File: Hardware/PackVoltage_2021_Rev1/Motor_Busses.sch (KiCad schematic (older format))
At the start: 40 parts, among them Q1 Q_NMOS_DGS, Q2 Q_NMOS_DGS, Q3 Q_NMOS_DGS, Q4 Q_NMOS_DGS, U2 LT1910, U3 LT1910, U4 LT1910, U5 INA281, U6 INA281, U7 INA281, U8 LT1910, U9 INA281

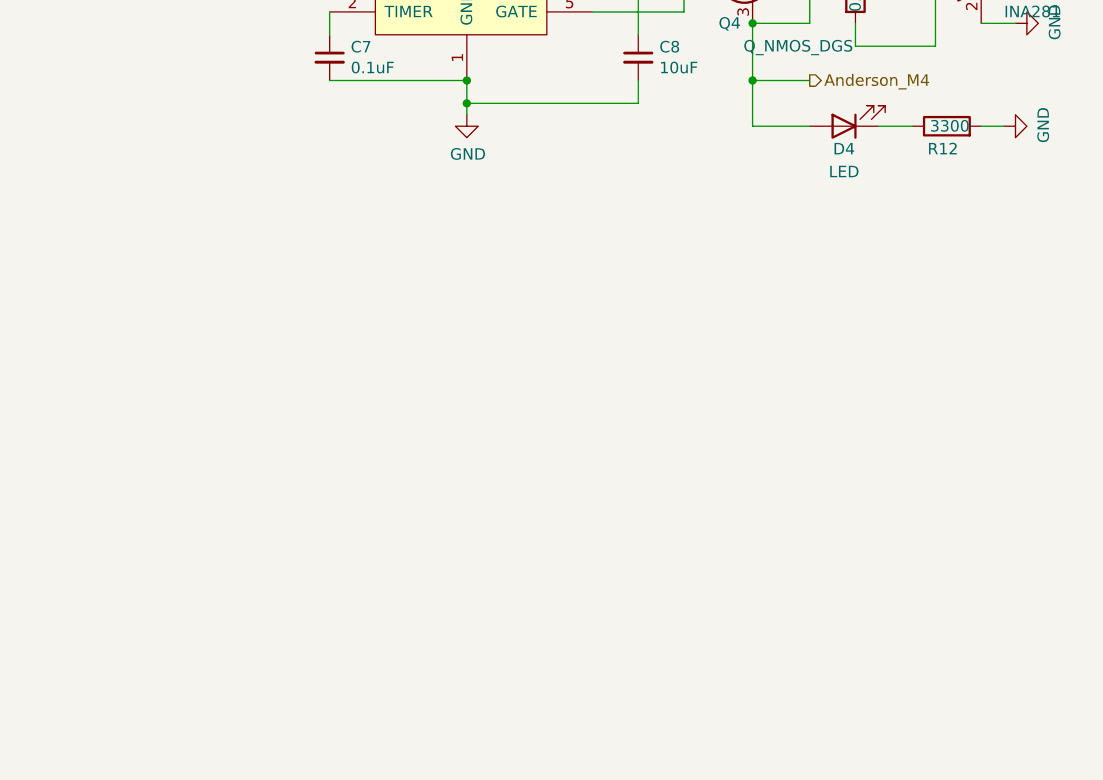
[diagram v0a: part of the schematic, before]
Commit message: Extra Bus, Connectors moved to top level
Added "Extra" 20A bus, tiva pins, and anderson
Moved molex connector out of tiva sheet so it is visible on top sheet
Removed "Power In" sheet to bring vias to top sheet.
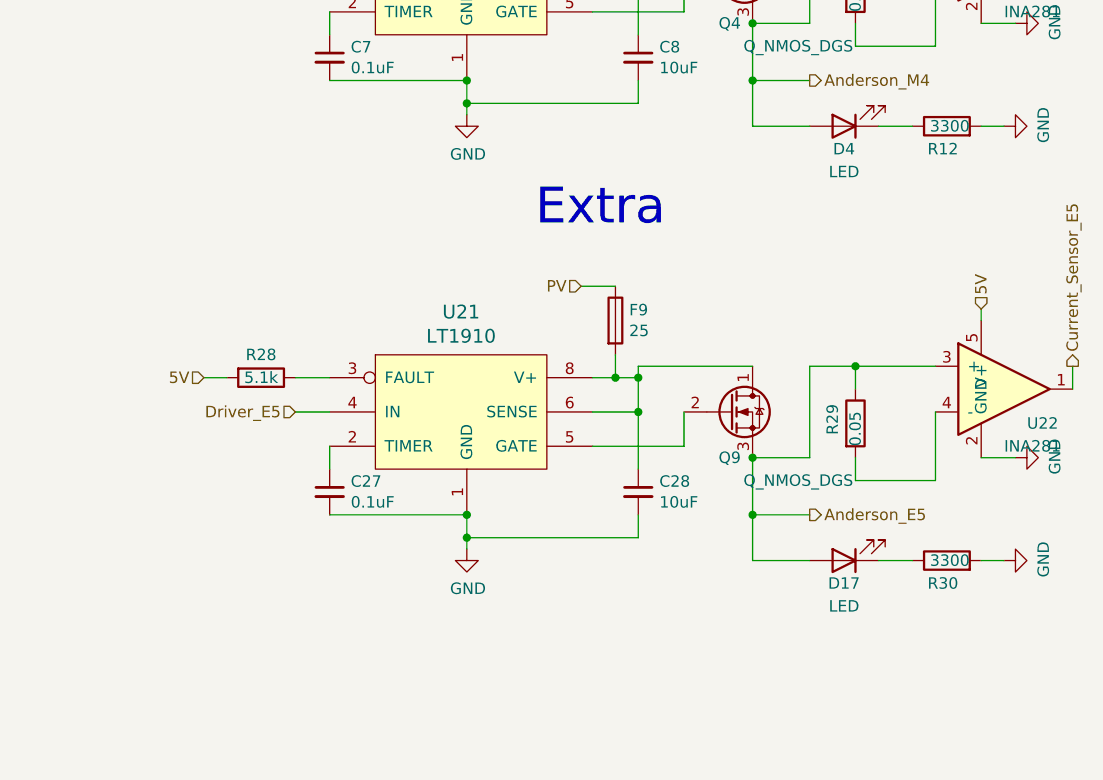
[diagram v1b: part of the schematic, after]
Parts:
- added C27: 0.1uF, symbol Device:C_Small
- added C28: 10uF, symbol Device:C_Small
- added D17: LED, symbol Device:LED
- added F9: 25, symbol Device:Fuse
- added Q9: Q_NMOS_DGS, symbol Device:Q_NMOS_DGS
- added R28: 5.1k, symbol Device:R
- added R29: 0.05, symbol Device:R
- added R30: 3300, symbol Device:R
- added U21: LT1910, symbol MRDT_ICs:LT1910
- added U22: INA281, symbol MRDT_ICs:INA281
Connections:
- net 5V: now also R28.2, U22.5 (V+)
- net GND: now also C27.2, C28.2, R30.2, U21.1 (GND), U22.2 (GND)
- net PV: now also F9.1
- new net: C28.1, F9.2, Q9.1 (D), U21.6 (SENSE), U21.8 (V+)
- new net: Q9.2 (G), U21.5 (GATE)
- new net: R28.1, U21.3 (FAULT)
- new net: C27.1, U21.2 (TIMER)
- new net: R29.2, U22.4 (-)
- new net: D17.1 (K), R30.1
- new net Anderson_E5: D17.2 (A), Q9.3 (S), R29.1, U22.3 (+)
- new net Current_Sensor_E5: U22.1
- new net Driver_E5: U21.4 (IN)
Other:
- note added: "Extra"

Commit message: Added 5th Motor
Added Motor 5 to Motor Busses, added tiva pins and anderson connections
Renamed Extra 5 to Extra 6
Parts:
- added C?: 0.1uF, symbol Device:C_Small
- added C?: 10uF, symbol Device:C_Small
- added D?: LED, symbol Device:LED
- added F?: 25, symbol Device:Fuse
- added Q?: Q_NMOS_DGS, symbol Device:Q_NMOS_DGS
- added R?: 5.1k, symbol Device:R
- added R?: 0.05, symbol Device:R
- added R?: 3300, symbol Device:R
- added U?: INA281, symbol MRDT_ICs:INA281
- added U?: LT1910, symbol MRDT_ICs:LT1910
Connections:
- net 5V: now also R?.2, U?.5 (V+)
- net GND: now also C?.2, C?.2, R?.2, U?.1 (GND), U?.2 (GND)
- net PV: now also F?.1
- net Anderson_E5 renamed Anderson_M5
- net Current_Sensor_E5 renamed Current_Sensor_M5
- net Driver_E5 renamed Driver_M5
- new net: C?.1, F?.2, Q?.1 (D), U?.6 (SENSE), U?.8 (V+)
- new net: Q?.2 (G), U?.5 (GATE)
- new net: R?.1, U?.3 (FAULT)
- new net: C?.1, U?.2 (TIMER)
- new net: R?.2, U?.4 (-)
- new net: D?.1 (K), R?.1
- new net Anderson_E6: D?.2 (A), Q?.3 (S), R?.1, U?.3 (+)
- new net Current_Sensor_E6: U?.1
- new net Driver_E6: U?.4 (IN)
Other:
- note added: "Motor 5"

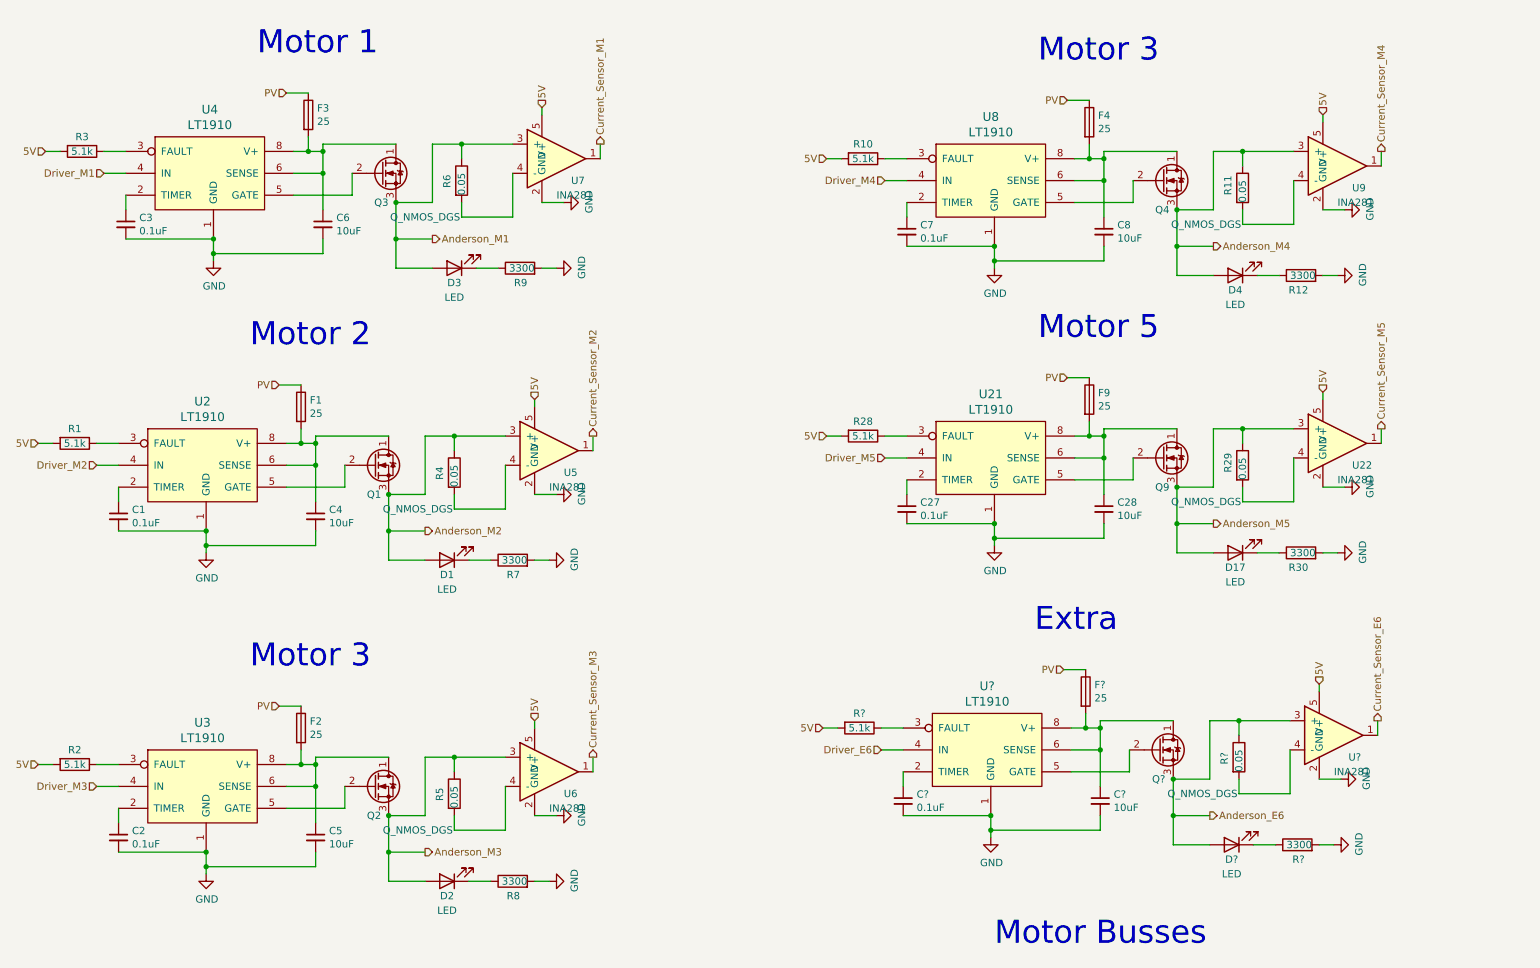
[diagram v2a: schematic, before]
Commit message: Renaming Extra Bus, Fixing Fuse Values
Renamed Extra 6 bus to Auxiliary 1 and moved it from Motor Busses to Other Busses
Changed Fuse values on Other Busses from 15 for all to 25 for Aux, Spare, and Rocket, to 10 for Vacuum, and to 20 for 12V
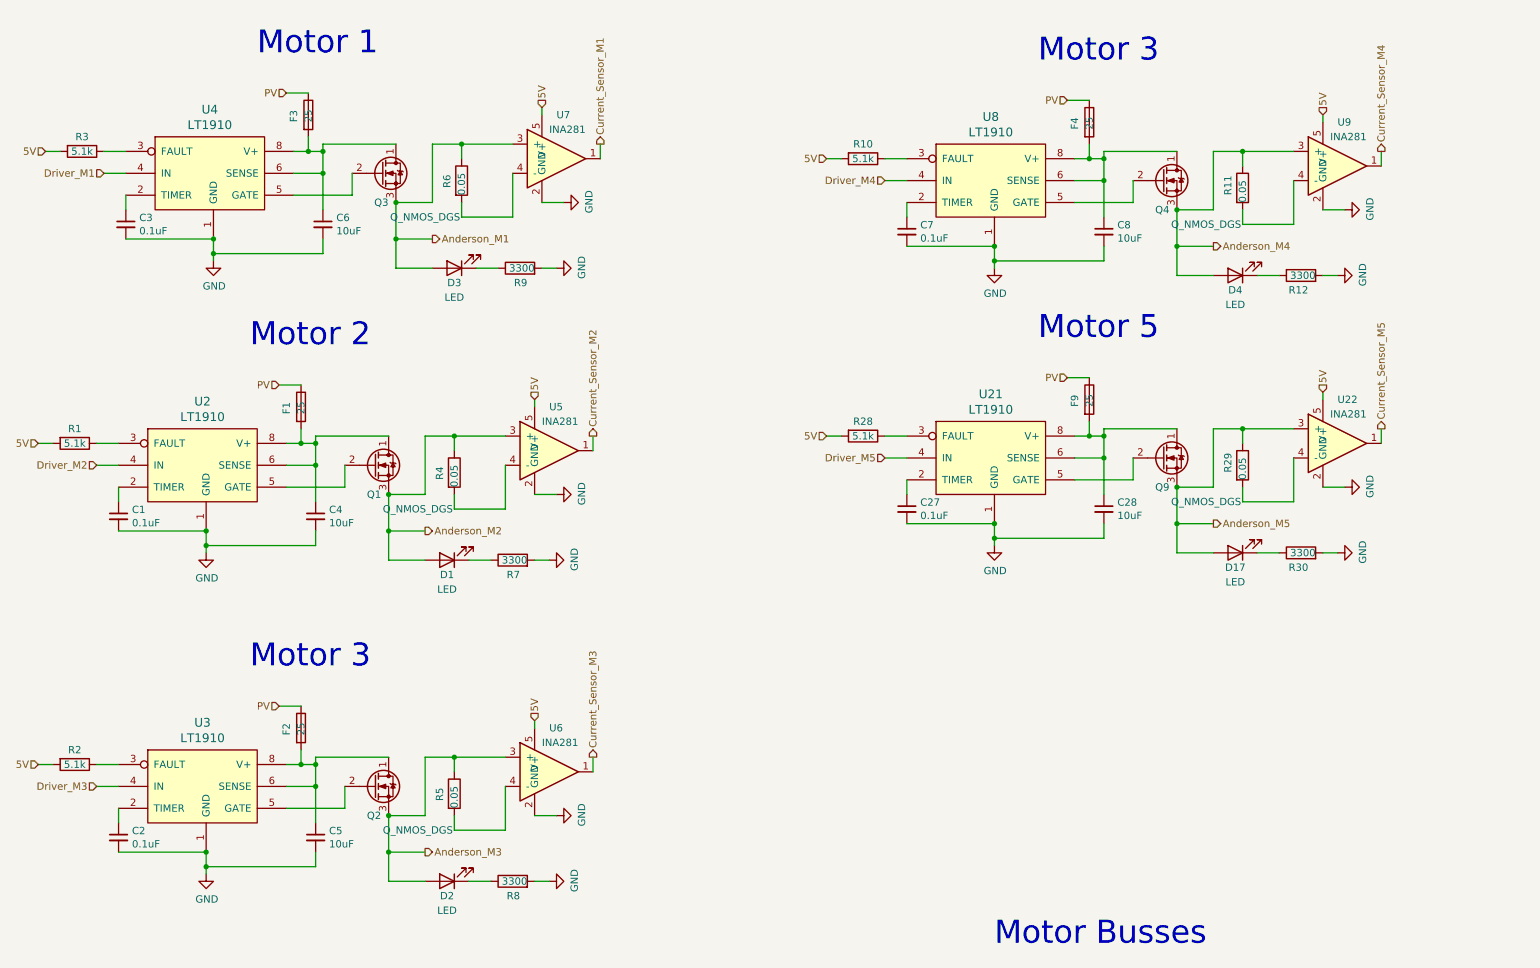
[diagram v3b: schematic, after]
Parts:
- removed C?: 0.1uF, symbol Device:C_Small
- removed C?: 10uF, symbol Device:C_Small
- removed D?: LED, symbol Device:LED
- removed F?: 25, symbol Device:Fuse
- removed Q?: Q_NMOS_DGS, symbol Device:Q_NMOS_DGS
- removed R?: 5.1k, symbol Device:R
- removed R?: 0.05, symbol Device:R
- removed R?: 3300, symbol Device:R
- removed U?: INA281, symbol MRDT_ICs:INA281
- removed U?: LT1910, symbol MRDT_ICs:LT1910
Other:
- note removed: "Extra"

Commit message: Fixed anderson connections
Mistake made when rearranging busses so they would fit on sheet fixed
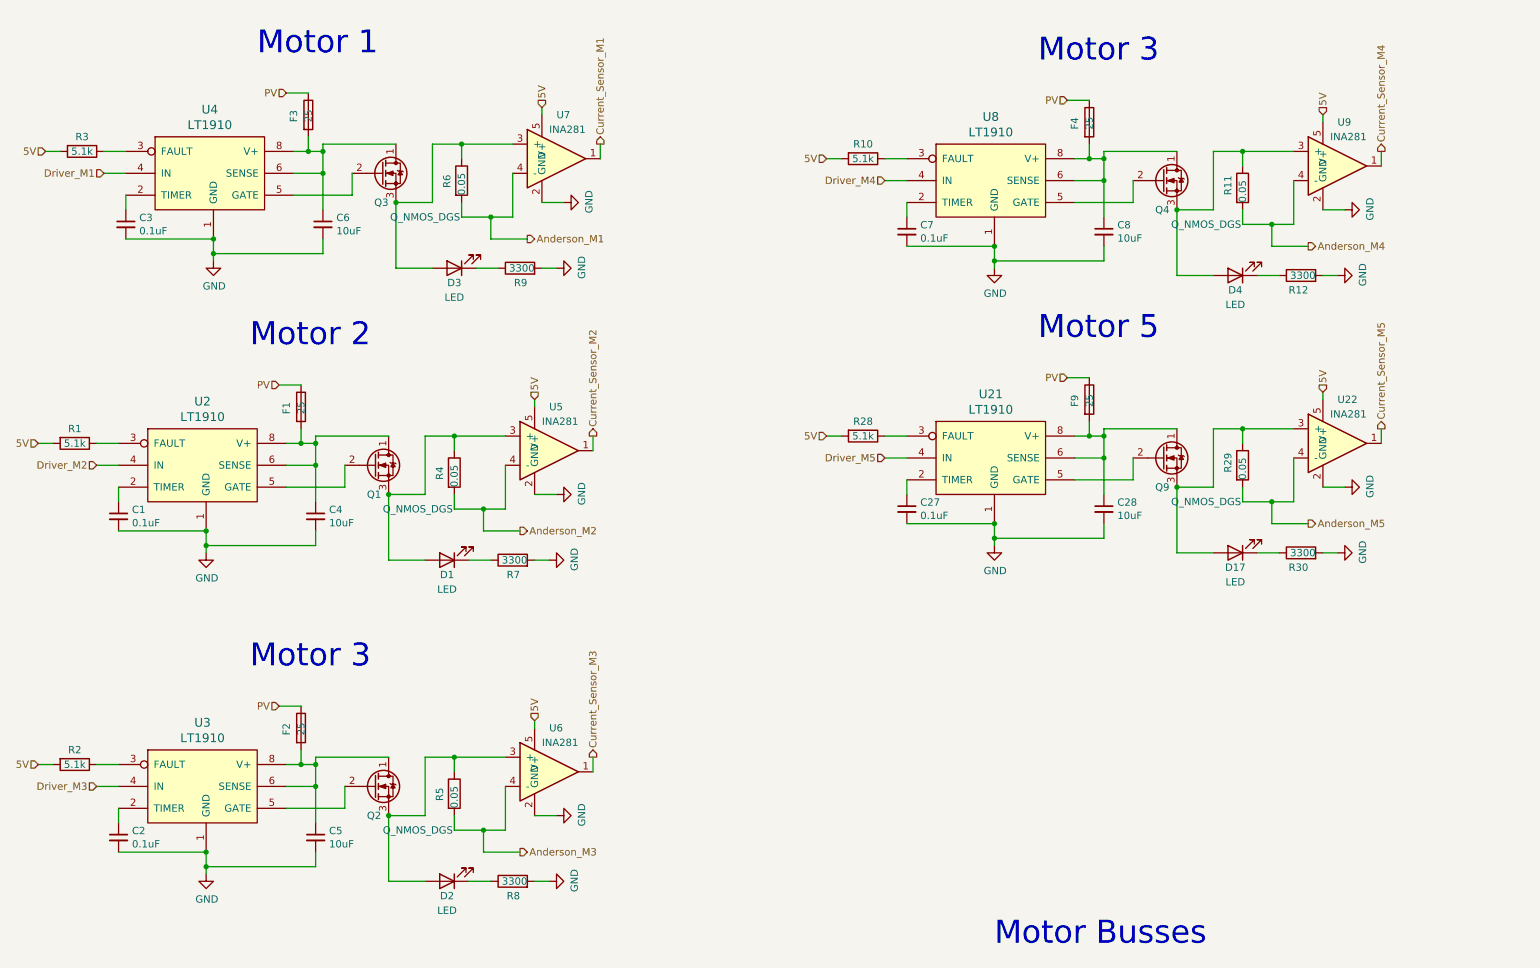
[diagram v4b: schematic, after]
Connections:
- net Anderson_M1: now also R6.2, U7.4 (-); no longer D3.2 (A), Q3.3 (S), R6.1, U7.3 (+)
- net Anderson_M2: now also R4.2, U5.4 (-); no longer D1.2 (A), Q1.3 (S), R4.1, U5.3 (+)
- net Anderson_M3: now also R5.2, U6.4 (-); no longer D2.2 (A), Q2.3 (S), R5.1, U6.3 (+)
- net Anderson_M4: now also R11.2, U9.4 (-); no longer D4.2 (A), Q4.3 (S), R11.1, U9.3 (+)
- net Anderson_M5: now also R29.2, U22.4 (-); no longer D17.2 (A), Q9.3 (S), R29.1, U22.3 (+)
- new net: D3.2 (A), Q3.3 (S), R6.1, U7.3 (+)
- new net: D17.2 (A), Q9.3 (S), R29.1, U22.3 (+)
- new net: D1.2 (A), Q1.3 (S), R4.1, U5.3 (+)
- new net: D2.2 (A), Q2.3 (S), R5.1, U6.3 (+)
- new net: D4.2 (A), Q4.3 (S), R11.1, U9.3 (+)
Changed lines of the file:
@@
 Connection ~ 3100 1850
 Wire Wire Line
-	3550 1950 3900 1950
-Wire Wire Line
-	3100 1850 3100 2100
-Wire Wire Line
-	3100 2100 3350 2100
-Connection ~ 3100 2100
-Wire Wire Line
-	3100 2100 3100 2300
+	3550 1950 3750 1950
+Wire Wire Line
+	3750 2100 4000 2100
 Text HLabel 4500 1450 1    50   Output ~ 0
 Current_Sensor_M1
@@
 Connection ~ 3050 3850
 Wire Wire Line
-	3500 3950 3850 3950
-Wire Wire Line
-	3050 3850 3050 4100
-Wire Wire Line
-	3050 4100 3300 4100
-Connection ~ 3050 4100
-Wire Wire Line
-	3050 4100 3050 4300
+	3500 3950 3700 3950
+Wire Wire Line
+	3700 4100 3950 4100
 Text HLabel 4450 3450 1    50   Output ~ 0
 Current_Sensor_M2
@@
 Connection ~ 3050 6050
 Wire Wire Line
-	3500 6150 3850 6150
-Wire Wire Line
-	3050 6050 3050 6300
-Wire Wire Line
-	3050 6300 3300 6300
-Connection ~ 3050 6300
-Wire Wire Line
-	3050 6300 3050 6500
+	3500 6150 3700 6150
+Wire Wire Line
+	3700 6300 3950 6300
 Text HLabel 4450 5650 1    50   Output ~ 0
 Current_Sensor_M3
@@
 Connection ~ 8450 1900
 Wire Wire Line
-	8900 2000 9250 2000
-Wire Wire Line
-	8450 1900 8450 2150
-Wire Wire Line
-	8450 2150 8700 2150
-Connection ~ 8450 2150
-Wire Wire Line
-	8450 2150 8450 2350
+	8900 2000 9100 2000
+Wire Wire Line
+	9100 2150 9350 2150
 Text HLabel 9850 1500 1    50   Output ~ 0
 Current_Sensor_M4
-Text HLabel 3350 2100 2    50   Output ~ 0
+Text HLabel 4000 2100 2    50   Output ~ 0
 Anderson_M1
-Text HLabel 3300 4100 2    50   Output ~ 0
+Text HLabel 3950 4100 2    50   Output ~ 0
 Anderson_M2
-Text HLabel 3300 6300 2    50   Output ~ 0
+Text HLabel 3950 6300 2    50   Output ~ 0
 Anderson_M3
-Text HLabel 8700 2150 2    50   Output ~ 0
+Text HLabel 9350 2150 2    50   Output ~ 0
 Anderson_M4
 $Comp
@@
 Connection ~ 8450 3800
 Wire Wire Line
-	8900 3900 9250 3900
-Wire Wire Line
-	8450 3800 8450 4050
-Wire Wire Line
-	8450 4050 8700 4050
-Connection ~ 8450 4050
-Wire Wire Line
-	8450 4050 8450 4250
+	8900 3900 9100 3900
+Wire Wire Line
+	9100 4050 9350 4050
 Text HLabel 9850 3400 1    50   Output ~ 0
 Current_Sensor_M5
-Text HLabel 8700 4050 2    50   Output ~ 0
+Text HLabel 9350 4050 2    50   Output ~ 0
 Anderson_M5
+Wire Wire Line
+	3100 1850 3100 2300
+Wire Wire Line
+	3750 1950 3750 2100
+Connection ~ 3750 1950
+Wire Wire Line
+	3750 1950 3900 1950
+Wire Wire Line
+	3050 3850 3050 4300
+Wire Wire Line
+	3700 4100 3700 3950
+Connection ~ 3700 3950
+Wire Wire Line
+	3700 3950 3850 3950
+Wire Wire Line
+	3050 6050 3050 6500
+Wire Wire Line
+	3700 6300 3700 6150
+Connection ~ 3700 6150
+Wire Wire Line
+	3700 6150 3850 6150
+Wire Wire Line
+	8450 3800 8450 4250
+Wire Wire Line
+	9100 4050 9100 3900
+Connection ~ 9100 3900
+Wire Wire Line
+	9100 3900 9250 3900
+Wire Wire Line
+	8450 1900 8450 2350
+Wire Wire Line
+	9100 2150 9100 2000
+Connection ~ 9100 2000
+Wire Wire Line
+	9100 2000 9250 2000
 $EndSCHEMATC
